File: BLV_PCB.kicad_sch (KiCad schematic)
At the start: 8 parts, among them J1 Cube0 JST-PH, J2 Cube0 JST-PH, J3 Cube0 JST-PH, J4 Micro_SD_Card

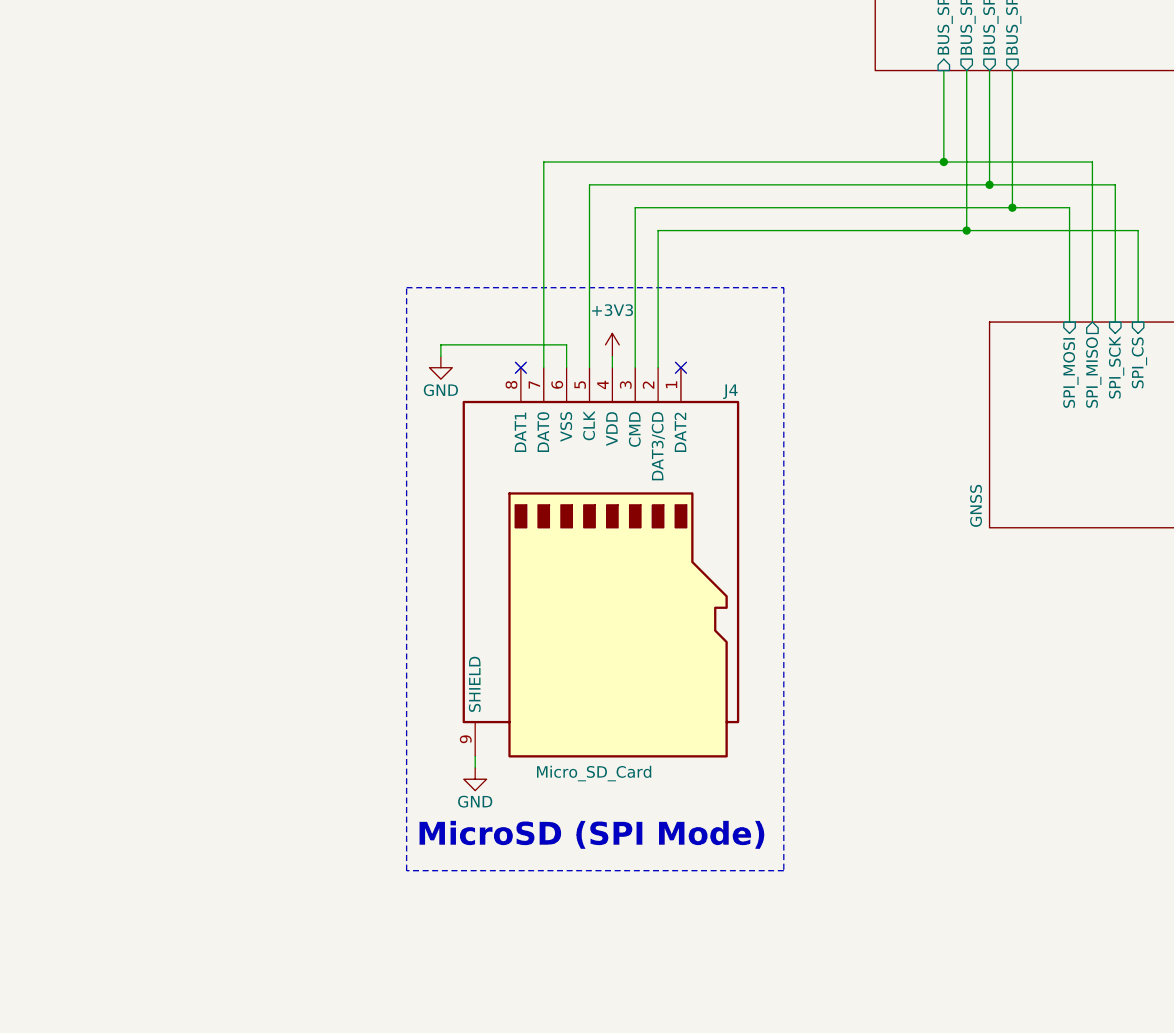
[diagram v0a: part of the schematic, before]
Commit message: Update BLV_PCB.kicad_sch
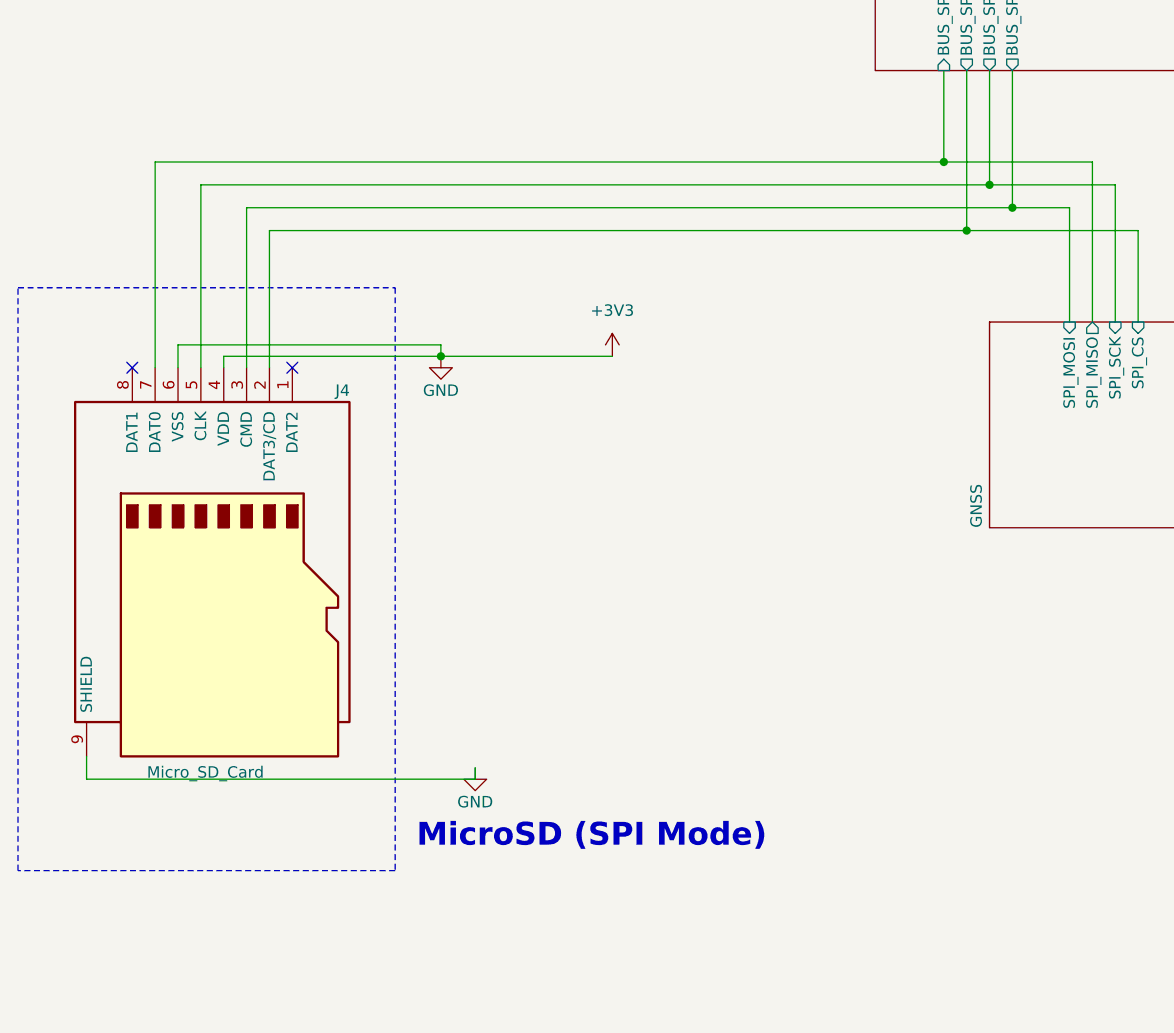
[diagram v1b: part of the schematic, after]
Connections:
- net GND is gone; now on net +3V3: J1.4 (Pin_4), J2.4 (Pin_4), J3.4 (Pin_4), J4.6 (VSS), J4.9 (SHIELD)
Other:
- moved on the sheet: J4
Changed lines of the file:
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@@
 	)
 	(rectangle
-		(start 87.63 168.91)
-		(end 129.54 233.68)
+		(start 44.45 168.91)
+		(end 86.36 233.68)
 		(stroke
 			(width 0)
@@
 		(color 0 0 0 0)
 	)
+	(junction
+		(at 91.44 176.53)
+		(diameter 0)
+		(color 0 0 0 0)
+	)
 	(no_connect
-		(at 118.11 177.8)
+		(at 74.93 177.8)
 	)
 	(no_connect
@@
 	)
 	(no_connect
-		(at 100.33 177.8)
+		(at 57.15 177.8)
 	)
 	(no_connect
@@
 	(wire
 		(pts
-			(xy 110.49 177.8) (xy 110.49 176.53)
+			(xy 67.31 177.8) (xy 67.31 176.53)
 		)
 		(stroke
@@
 	(wire
 		(pts
-			(xy 154.94 160.02) (xy 113.03 160.02)
+			(xy 67.31 176.53) (xy 91.44 176.53)
+		)
+		(stroke
+			(width 0)
+			(type default)
+		)
+	)
+	(wire
+		(pts
+			(xy 154.94 160.02) (xy 69.85 160.02)
 		)
 		(stroke
@@
 	(wire
 		(pts
-			(xy 115.57 162.56) (xy 115.57 177.8)
+			(xy 72.39 162.56) (xy 72.39 177.8)
 		)
 		(stroke
@@
 	(wire
 		(pts
-			(xy 102.87 154.94) (xy 102.87 177.8)
+			(xy 59.69 154.94) (xy 59.69 177.8)
 		)
 		(stroke
@@
 	(wire
 		(pts
-			(xy 105.41 175.26) (xy 91.44 175.26)
+			(xy 62.23 175.26) (xy 91.44 175.26)
 		)
 		(stroke
@@
 	(wire
 		(pts
-			(xy 95.25 220.98) (xy 95.25 222.25)
+			(xy 52.07 220.98) (xy 52.07 223.52)
 		)
 		(stroke
@@
 	(wire
 		(pts
-			(xy 113.03 160.02) (xy 113.03 177.8)
+			(xy 69.85 160.02) (xy 69.85 177.8)
 		)
 		(stroke
@@
 	(wire
 		(pts
-			(xy 152.4 157.48) (xy 107.95 157.48)
+			(xy 152.4 157.48) (xy 64.77 157.48)
 		)
 		(stroke
@@
 	(wire
 		(pts
-			(xy 149.86 162.56) (xy 115.57 162.56)
-		)
-		(stroke
-			(width 0)
-			(type default)
-		)
-	)
-	(wire
-		(pts
-			(xy 105.41 177.8) (xy 105.41 175.26)
+			(xy 149.86 162.56) (xy 72.39 162.56)
+		)
+		(stroke
+			(width 0)
+			(type default)
+		)
+	)
+	(wire
+		(pts
+			(xy 62.23 177.8) (xy 62.23 175.26)
 		)
 		(stroke
@@
 	(wire
 		(pts
+			(xy 52.07 223.52) (xy 95.25 223.52)
+		)
+		(stroke
+			(width 0)
+			(type default)
+		)
+	)
+	(wire
+		(pts
 			(xy 124.46 107.95) (xy 130.81 107.95)
 		)
@@
 	(wire
 		(pts
-			(xy 107.95 157.48) (xy 107.95 177.8)
+			(xy 64.77 157.48) (xy 64.77 177.8)
 		)
 		(stroke
@@
 	(wire
 		(pts
-			(xy 147.32 154.94) (xy 102.87 154.94)
+			(xy 147.32 154.94) (xy 59.69 154.94)
 		)
 		(stroke
@@
 		(pts
 			(xy 149.86 144.78) (xy 149.86 162.56)
+		)
+		(stroke
+			(width 0)
+			(type default)
+		)
+	)
+	(wire
+		(pts
+			(xy 91.44 176.53) (xy 110.49 176.53)
+		)
+		(stroke
+			(width 0)
+			(type default)
+		)
+	)
+	(wire
+		(pts
+			(xy 95.25 223.52) (xy 95.25 222.25)
 		)
 		(stroke
@@
 	(symbol
 		(lib_id "Connector:Micro_SD_Card")
-		(at 110.49 200.66 270)
+		(at 67.31 200.66 270)
 		(unit 1)
 		(exclude_from_sim no)
@@
 		(dnp no)
 		(property "Reference" "J4"
-			(at 123.698 180.34 90)
+			(at 80.518 180.34 90)
 			(effects
 				(font
@@
 		)
 		(property "Value" "Micro_SD_Card"
-			(at 108.458 222.758 90)
+			(at 65.278 222.758 90)
 			(effects
 				(font
@@
 		)
 		(property "Footprint" "Connector_Card:microSD_HC_Wuerth_693072010801"
-			(at 118.11 229.87 0)
+			(at 74.93 229.87 0)
 			(effects
 				(font
@@
 		)
 		(property "Datasheet" "https://www.we-online.com/components/products/datasheet/693072010801.pdf"
-			(at 110.49 200.66 0)
+			(at 67.31 200.66 0)
 			(effects
 				(font
@@
 		)
 		(property "Description" "Micro SD Card Socket | https://elm-chan.org/docs/mmc/mmc_e.html"
-			(at 110.49 200.66 0)
-			(effects
-				(font
+			(at 67.31 200.66 0)
+			(effects
+				(font
